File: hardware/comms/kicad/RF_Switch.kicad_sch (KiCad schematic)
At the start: 12 parts, among them U11 PE4259, U12 TLV75530PDBVR, U13 SN74LVC1G17DBVR

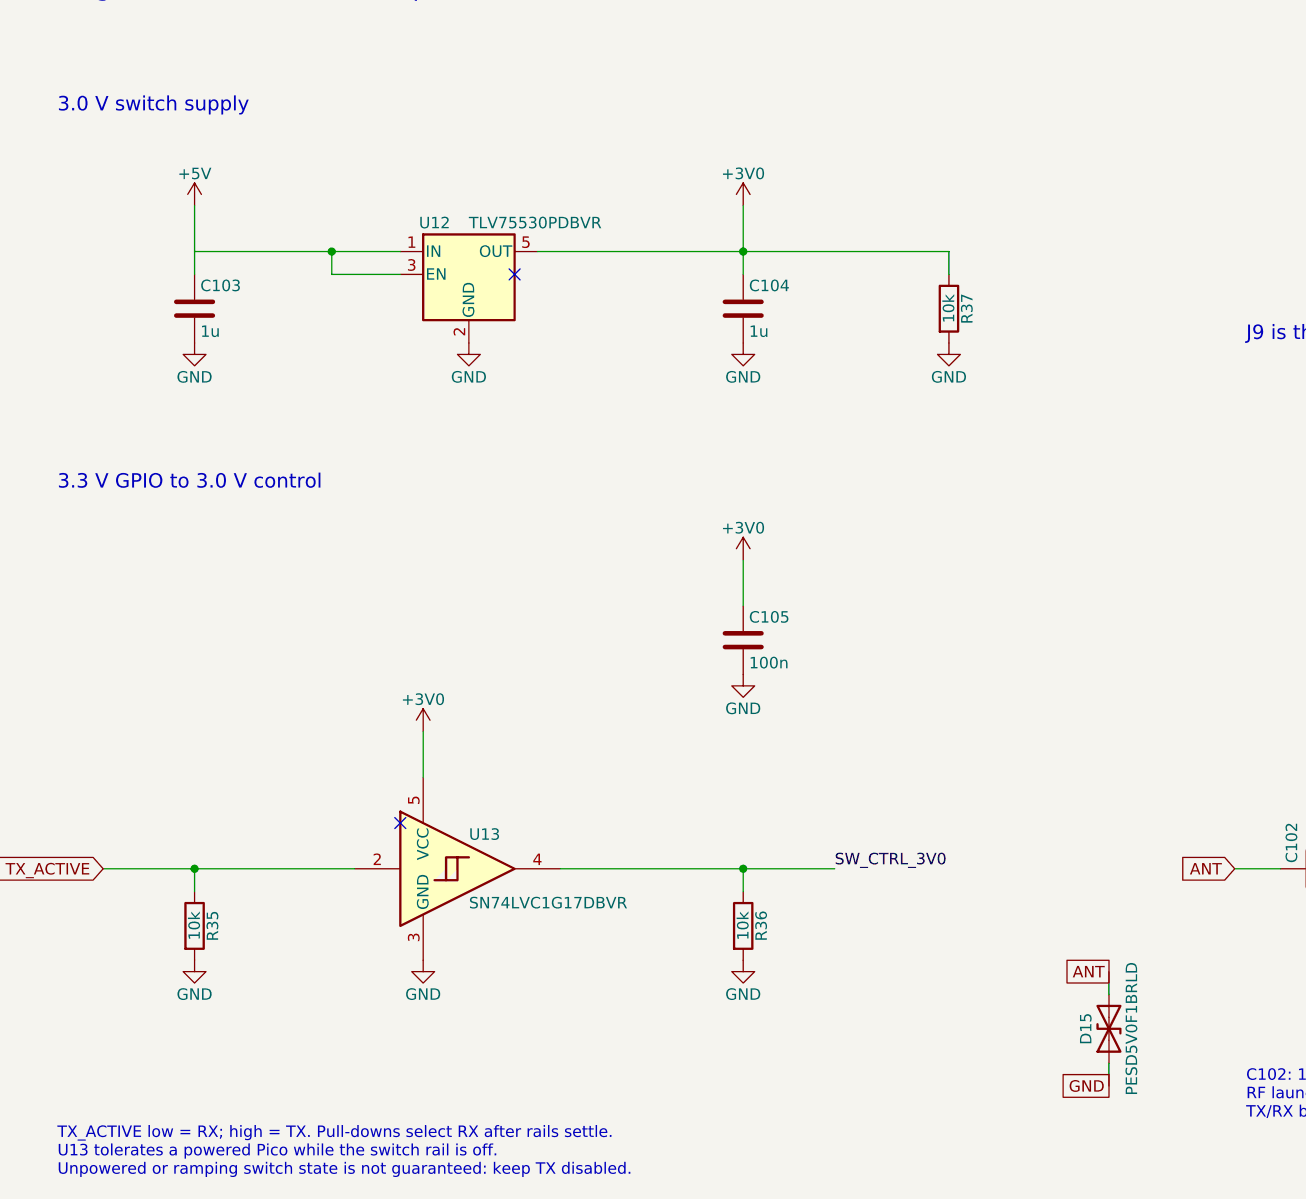
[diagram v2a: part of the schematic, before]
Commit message: Complete dual-CAN transceiver hardware prototype
Preserve the current transceiver schematics, PCB, libraries and validation evidence as a focused hardware review against main.
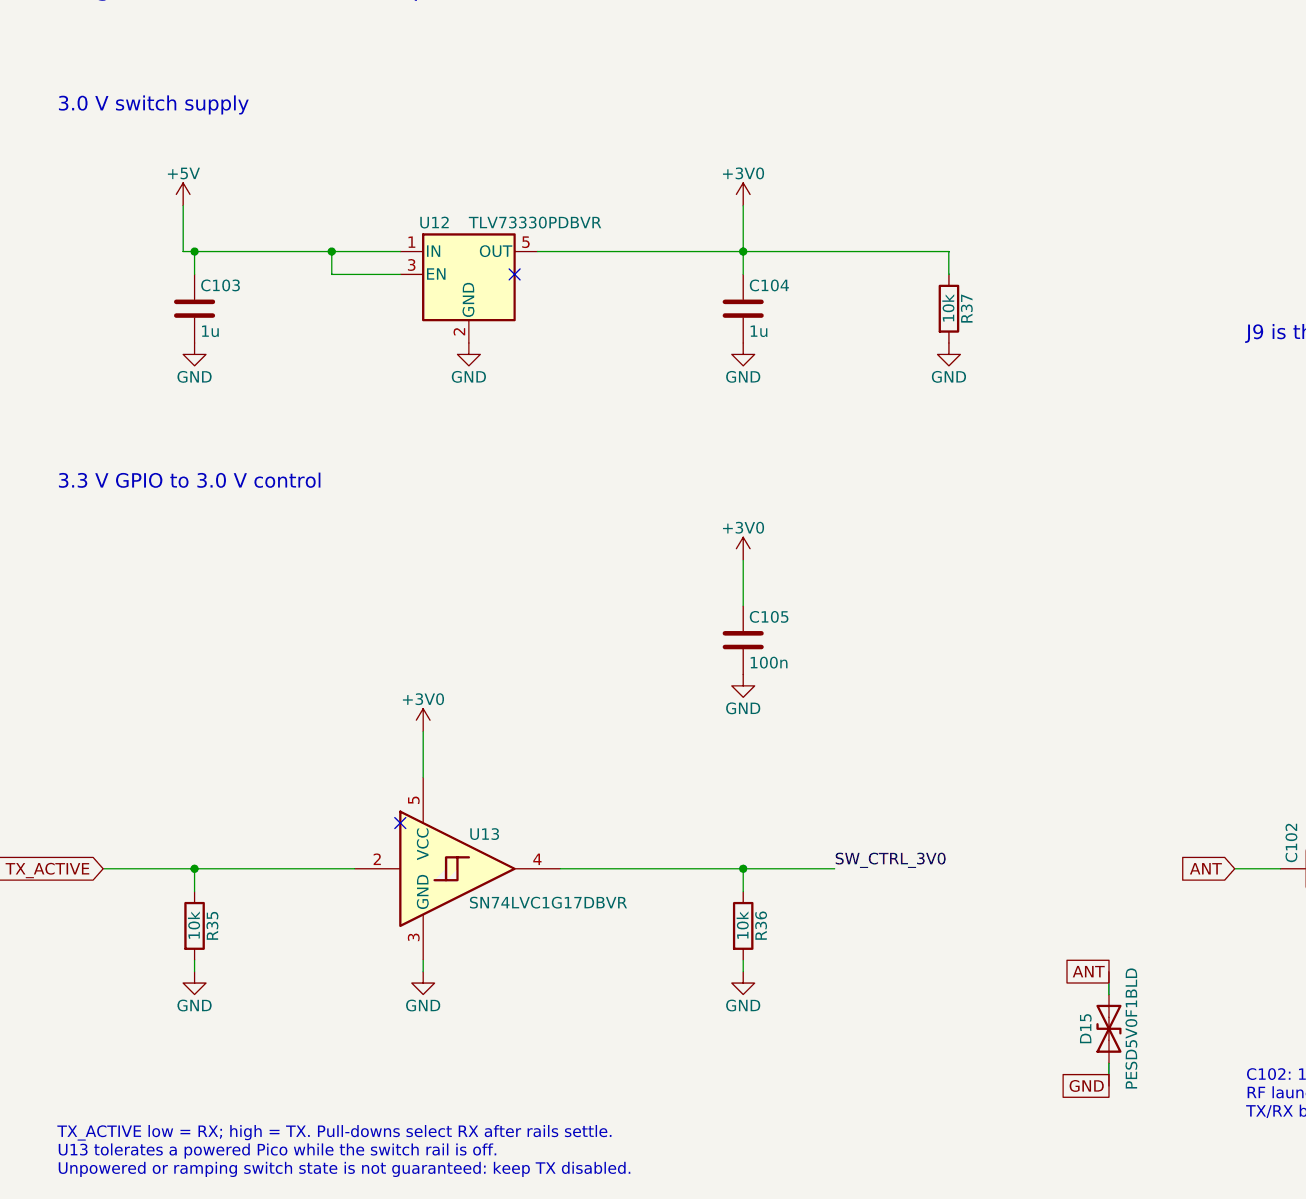
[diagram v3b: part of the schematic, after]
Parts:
- D15: value PESD5V0F1BRLD -> PESD5V0F1BLD; LCSC Part # (none) -> C478204; MPN PESD5V0F1BRLD -> PESD5V0F1BLD,315; Manufacturer Part # (none) -> PESD5V0F1BLD,315; Qualification (none) -> Prototype selection; see verification/components/prototype_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
- U12: value TLV75530PDBVR -> TLV73330PDBVR; symbol Regulator_Linear:TLV75530PDBV -> Regulator_Linear:TLV73330PDBV; LCSC Part # C507268 -> C882826; MPN TLV75530PDBVR -> TLV73330PDBVR; Manufacturer (none) -> Texas Instruments; Manufacturer Part # TLV75530PDBVR -> TLV73330PDBVR
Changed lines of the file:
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@@
 	(generator_version "10.0")
 	(paper "A4")
+	(title_block
+		(comment 9 "UHF/UHF revision in review - not for fabrication")
+	)
 	(text "3.0 V switch supply"
 		(exclude_from_sim no)
@@
 		(color 0 0 0 0)
 	)
+	(junction
+		(at 40.64 48.26)
+		(diameter 0)
+		(color 0 0 0 0)
+	)
 	(no_connect
 		(at 76.2 50.8)
@@
 	(wire
 		(pts
+			(xy 66.04 128.27) (xy 66.04 127)
+		)
+		(stroke
+			(width 0)
+			(type default)
+		)
+	)
+	(wire
+		(pts
 			(xy 187.96 121.92) (xy 180.34 121.92)
 		)
@@
 	(wire
 		(pts
+			(xy 40.64 128.27) (xy 40.64 127)
+		)
+		(stroke
+			(width 0)
+			(type default)
+		)
+	)
+	(wire
+		(pts
 			(xy 124.46 48.26) (xy 124.46 50.8)
 		)
@@
 	(wire
 		(pts
+			(xy 40.64 48.26) (xy 39.37 48.26)
+		)
+		(stroke
+			(width 0)
+			(type default)
+		)
+	)
+	(wire
+		(pts
 			(xy 101.6 87.63) (xy 101.6 82.55)
 		)
@@
 	(wire
 		(pts
+			(xy 101.6 128.27) (xy 101.6 127)
+		)
+		(stroke
+			(width 0)
+			(type default)
+		)
+	)
+	(wire
+		(pts
 			(xy 101.6 48.26) (xy 101.6 43.18)
 		)
@@
 	(wire
 		(pts
-			(xy 40.64 48.26) (xy 40.64 43.18)
+			(xy 39.37 48.26) (xy 39.37 43.18)
 		)
 		(stroke
@@
 	)
 	(symbol
-		(lib_id "Regulator_Linear:TLV75530PDBV")
+		(lib_id "Regulator_Linear:TLV73330PDBV")
 		(at 71.12 50.8 0)
 		(unit 1)
@@
 			)
 		)
-		(property "Value" "TLV75530PDBVR"
+		(property "Value" "TLV73330PDBVR"
 			(at 71.12 45.085 0)
 			(show_name no)
@@
 			)
 		)
-		(property "Datasheet" "http://www.ti.com/lit/ds/symlink/tlv755p.pdf"
+		(property "Datasheet" "https://www.ti.com/lit/ds/symlink/tlv733p.pdf"
 			(at 71.12 50.8 0)
 			(hide yes)
@@
 			)
 		)
-		(property "Description" "500mA Low Dropout Voltage Regulator, Fixed Output 3.0V, SOT-23-5"
+		(property "Description" "3.0 V 300 mA LDO, SOT-23-5"
 			(at 71.12 50.8 0)
 			(hide yes)
@@
 			)
 		)
-		(property "MPN" "TLV75530PDBVR"
+		(property "MPN" "TLV73330PDBVR"
 			(at 71.12 50.8 0)
 			(hide yes)
@@
 			)
 		)
-		(property "LCSC Part #" "C507268"
+		(property "LCSC Part #" "C882826"
 			(at 71.12 50.8 0)
 			(hide yes)
@@
 			)
 		)
-		(property "Manufacturer Part #" "TLV75530PDBVR"
+		(property "Manufacturer Part #" "TLV73330PDBVR"
+			(at 71.12 50.8 0)
+			(hide yes)
+			(show_name no)
+			(do_not_autoplace no)
+			(effects
+				(font
+					(size 1.27 1.27)
+				)
+			)
+		)
+		(property "Manufacturer" "Texas Instruments"
 			(at 71.12 50.8 0)
 			(hide yes)
@@
 	(symbol
 		(lib_id "power:GND")
-		(at 101.6 127 0)
+		(at 101.6 128.27 0)
 		(unit 1)
 		(body_style 1)
@@
 		(dnp no)
 		(property "Reference" "#PWR009"
-			(at 101.6 133.35 0)
+			(at 101.6 134.62 0)
 			(hide yes)
 			(show_name no)
@@
 		)
 		(property "Value" "GND"
-			(at 101.6 130.81 0)
+			(at 101.6 132.08 0)
 			(show_name no)
 			(do_not_autoplace no)
@@
 		)
 		(property "Footprint" ""
-			(at 101.6 127 0)
+			(at 101.6 128.27 0)
 			(hide yes)
 			(show_name no)
@@
 		)
 		(property "Datasheet" ""
-			(at 101.6 127 0)
+			(at 101.6 128.27 0)
 			(hide yes)
 			(show_name no)
@@
 		)
 		(property "Description" "Power symbol creates a global label with name \"GND\" , ground"
-			(at 101.6 127 0)
+			(at 101.6 128.27 0)
 			(hide yes)
 			(show_name no)
@@
 	(symbol
 		(lib_id "power:+5V")
-		(at 40.64 43.18 0)
+		(at 39.37 43.18 0)
 		(unit 1)
 		(body_style 1)
@@
 		(dnp no)
 		(property "Reference" "#PWR001"
-			(at 40.64 46.99 0)
+			(at 39.37 46.99 0)
 			(hide yes)
 			(show_name no)
@@
 		)
 		(property "Value" "+5V"
-			(at 40.64 39.624 0)
+			(at 39.37 39.624 0)
 			(show_name no)
 			(do_not_autoplace no)
@@
 		)
 		(property "Footprint" ""
-			(at 40.64 43.18 0)
+			(at 39.37 43.18 0)
 			(hide yes)
 			(show_name no)
@@
 		)
 		(property "Datasheet" ""
-			(at 40.64 43.18 0)
+			(at 39.37 43.18 0)
 			(hide yes)
 			(show_name no)
@@
 		)
 		(property "Description" "Power symbol creates a global label with name \"+5V\""
-			(at 40.64 43.18 0)
+			(at 39.37 43.18 0)
 			(hide yes)
 			(show_name no)
@@
 			)
 		)
-		(property "Value" "PESD5V0F1BRLD"
+		(property "Value" "PESD5V0F1BLD"
 			(at 144.78 134.62 0)
 			(show_name no)
@@
 			)
 		)
-		(property "Datasheet" "https://assets.nexperia.com/documents/data-sheet/PESD5V0F1BRLD.pdf"
+		(property "Datasheet" "https://assets.nexperia.com/documents/data-sheet/PESD5V0F1BLD.pdf"
 			(at 142.24 134.62 0)
 			(hide yes)
@@
 			)
 		)
-		(property "MPN" "PESD5V0F1BRLD"
+		(property "MPN" "PESD5V0F1BLD,315"
 			(at 142.24 134.62 0)
 			(hide yes)
@@
 			)
 		)
+		(property "LCSC Part #" "C478204"
+			(at 142.24 134.62 0)
+			(hide yes)
+			(show_name no)
+			(do_not_autoplace no)
+			(effects
+				(font
+					(size 1.27 1.27)
+				)
+			)
+		)
+		(property "Manufacturer Part #" "PESD5V0F1BLD,315"
+			(at 142.24 134.62 0)
+			(hide yes)
+			(show_name no)
+			(do_not_autoplace no)
+			(effects
+				(font
+					(size 1.27 1.27)
+				)
+			)
+		)
+		(property "Qualification" "Prototype selection; see verification/components/prototype_parts_2026-10-03.md"
+			(at 142.24 134.62 0)
+			(hide yes)
+			(show_name no)
+			(do_not_autoplace no)
+			(effects
+				(font
+					(size 1.27 1.27)
+				)
+			)
+		)
 		(pin "2"
 		)
@@
 	(symbol
 		(lib_id "power:GND")
-		(at 66.04 127 0)
+		(at 66.04 128.27 0)
 		(unit 1)
 		(body_style 1)
@@
 		(dnp no)
 		(property "Reference" "#PWR008"
-			(at 66.04 133.35 0)
+			(at 66.04 134.62 0)
 			(hide yes)
 			(show_name no)
@@
 		)
 		(property "Value" "GND"
-			(at 66.04 130.81 0)
+			(at 66.04 132.08 0)
 			(show_name no)
 			(do_not_autoplace no)
@@
 		)
 		(property "Footprint" ""
-			(at 66.04 127 0)
+			(at 66.04 128.27 0)
 			(hide yes)
 			(show_name no)
@@
 		)
 		(property "Datasheet" ""
-			(at 66.04 127 0)
+			(at 66.04 128.27 0)
 			(hide yes)
 			(show_name no)
@@
 		)
 		(property "Description" "Power symbol creates a global label with name \"GND\" , ground"
-			(at 66.04 127 0)
+			(at 66.04 128.27 0)
 			(hide yes)
 			(show_name no)
@@
 	(symbol
 		(lib_id "power:GND")
-		(at 40.64 127 0)
+		(at 40.64 128.27 0)
 		(unit 1)
 		(body_style 1)
@@
 		(dnp no)
 		(property "Reference" "#PWR007"
-			(at 40.64 133.35 0)
+			(at 40.64 134.62 0)
 			(hide yes)
 			(show_name no)
@@
 		)
 		(property "Value" "GND"
-			(at 40.64 130.81 0)
+			(at 40.64 132.08 0)
 			(show_name no)
 			(do_not_autoplace no)
@@
 		)
 		(property "Footprint" ""
-			(at 40.64 127 0)
+			(at 40.64 128.27 0)
 			(hide yes)
 			(show_name no)
@@
 		)
 		(property "Datasheet" ""
-			(at 40.64 127 0)
+			(at 40.64 128.27 0)
 			(hide yes)
 			(show_name no)
@@
 		)
 		(property "Description" "Power symbol creates a global label with name \"GND\" , ground"
-			(at 40.64 127 0)
+			(at 40.64 128.27 0)
 			(hide yes)
 			(show_name no)
